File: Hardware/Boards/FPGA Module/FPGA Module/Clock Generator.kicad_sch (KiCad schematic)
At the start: 20 parts, among them U21 Si5338A-B-GMR, Y2 12Mhz

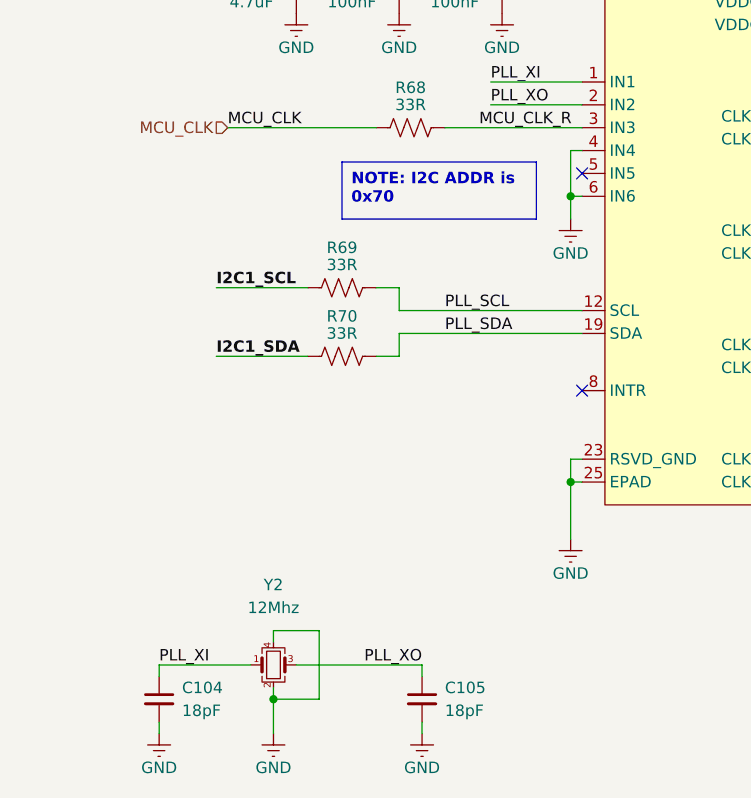
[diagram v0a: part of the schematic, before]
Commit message: updated fpga module schematics
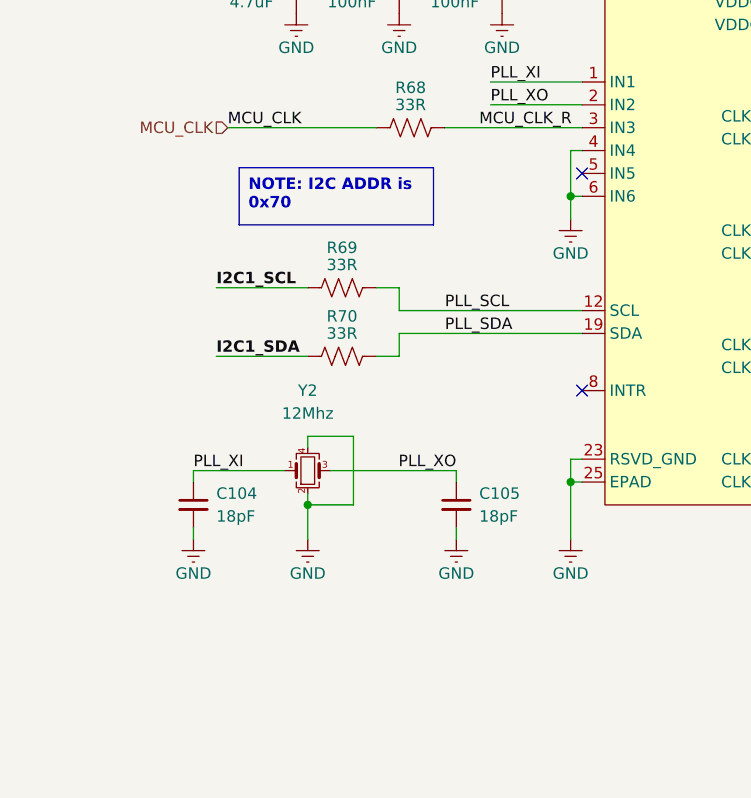
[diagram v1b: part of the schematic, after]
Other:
- moved on the sheet: C104, C105, Y2
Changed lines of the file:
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@@
 	)
 	(junction
-		(at 166.37 186.69)
+		(at 170.18 165.1)
 		(diameter 0)
 		(color 0 0 0 0)
@@
 	(wire
 		(pts
-			(xy 166.37 186.69) (xy 166.37 190.5)
+			(xy 170.18 165.1) (xy 170.18 168.91)
 		)
 		(stroke
@@
 	(wire
 		(pts
-			(xy 153.67 182.88) (xy 163.83 182.88)
+			(xy 157.48 161.29) (xy 167.64 161.29)
 		)
 		(stroke
@@
 	(wire
 		(pts
-			(xy 171.45 179.07) (xy 171.45 186.69)
+			(xy 175.26 157.48) (xy 175.26 165.1)
 		)
 		(stroke
@@
 	(wire
 		(pts
-			(xy 166.37 186.69) (xy 166.37 185.42)
+			(xy 170.18 165.1) (xy 170.18 163.83)
 		)
 		(stroke
@@
 	(wire
 		(pts
-			(xy 171.45 186.69) (xy 166.37 186.69)
+			(xy 175.26 165.1) (xy 170.18 165.1)
 		)
 		(stroke
@@
 	(wire
 		(pts
-			(xy 153.67 189.23) (xy 153.67 190.5)
+			(xy 157.48 167.64) (xy 157.48 168.91)
 		)
 		(stroke
@@
 	(wire
 		(pts
-			(xy 182.88 189.23) (xy 182.88 190.5)
+			(xy 186.69 167.64) (xy 186.69 168.91)
 		)
 		(stroke
@@
 	(wire
 		(pts
-			(xy 166.37 180.34) (xy 166.37 179.07)
+			(xy 170.18 158.75) (xy 170.18 157.48)
 		)
 		(stroke
@@
 	(wire
 		(pts
-			(xy 182.88 182.88) (xy 182.88 184.15)
+			(xy 186.69 161.29) (xy 186.69 162.56)
 		)
 		(stroke
@@
 	(wire
 		(pts
-			(xy 168.91 182.88) (xy 182.88 182.88)
+			(xy 172.72 161.29) (xy 186.69 161.29)
 		)
 		(stroke
@@
 	(wire
 		(pts
-			(xy 166.37 179.07) (xy 171.45 179.07)
+			(xy 170.18 157.48) (xy 175.26 157.48)
 		)
 		(stroke
@@
 	(wire
 		(pts
-			(xy 153.67 182.88) (xy 153.67 184.15)
+			(xy 157.48 161.29) (xy 157.48 162.56)
 		)
 		(stroke
@@
 	(text_box "NOTE: I2C ADDR is 0x70"
 		(exclude_from_sim no)
-		(at 173.99 127 0)
+		(at 162.56 127.635 0)
 		(size 21.59 6.35)
 		(stroke
@@
 	)
 	(label "PLL_XI"
-		(at 153.67 182.88 0)
+		(at 157.48 161.29 0)
 		(fields_autoplaced yes)
 		(effects
@@
 	)
 	(label "PLL_XO"
-		(at 182.88 182.88 180)
+		(at 186.69 161.29 180)
 		(fields_autoplaced yes)
 		(effects
@@
 	(symbol
 		(lib_id "Device:Crystal_GND24_Small")
-		(at 166.37 182.88 0)
+		(at 170.18 161.29 0)
 		(unit 1)
 		(exclude_from_sim no)
@@
 		(dnp no)
 		(property "Reference" "Y2"
-			(at 166.37 173.99 0)
+			(at 170.18 152.4 0)
 			(effects
 				(font
@@
 		)
 		(property "Value" "12Mhz"
-			(at 166.37 176.53 0)
+			(at 170.18 154.94 0)
 			(effects
 				(font
@@
 		)
 		(property "Footprint" "Oscillator:Oscillator_SMD_Abracon_ASE-4Pin_3.2x2.5mm"
-			(at 166.37 182.88 0)
+			(at 170.18 161.29 0)
 			(effects
 				(font
@@
 		)
 		(property "Datasheet" "https://abracon.com/Resonators/abm8.pdf"
-			(at 166.37 182.88 0)
+			(at 170.18 161.29 0)
 			(effects
 				(font
@@
 		)
 		(property "Description" "Four pin crystal, GND on pins 2 and 4, small symbol"
-			(at 166.37 182.88 0)
+			(at 170.18 161.29 0)
 			(effects
 				(font
@@
 	(symbol
 		(lib_id "Device:C_Small")
-		(at 182.88 186.69 0)
+		(at 186.69 165.1 0)
 		(unit 1)
 		(exclude_from_sim no)
@@
 		(fields_autoplaced yes)
 		(property "Reference" "C105"
-			(at 185.42 185.4262 0)
+			(at 189.23 163.8362 0)
 			(effects
 				(font
@@
 		)
 		(property "Value" "18pF"
-			(at 185.42 187.9662 0)
+			(at 189.23 166.3762 0)
 			(effects
 				(font
@@
 		)
 		(property "Footprint" "Capacitor_SMD:C_0201_0603Metric"
-			(at 182.88 186.69 0)
+			(at 186.69 165.1 0)
 			(effects
 				(font
@@
 		)
 		(property "Datasheet" "~"
-			(at 182.88 186.69 0)
+			(at 186.69 165.1 0)
 			(effects
 				(font
@@
 		)
 		(property "Description" "Unpolarized capacitor, small symbol"
-			(at 182.88 186.69 0)
+			(at 186.69 165.1 0)
 			(effects
 				(font
@@
 	(symbol
 		(lib_id "power:GND")
-		(at 153.67 190.5 0)
+		(at 157.48 168.91 0)
 		(unit 1)
 		(exclude_from_sim no)
@@
 		(dnp no)
 		(property "Reference" "#PWR0198"
-			(at 153.67 194.31 0)
+			(at 157.48 172.72 0)
 			(effects
 				(font
@@
 		)
 		(property "Value" "GND"
-			(at 153.67 194.31 0)
+			(at 157.48 172.72 0)
 			(effects
 				(font
@@
 		)
 		(property "Footprint" ""
-			(at 153.67 190.5 0)
+			(at 157.48 168.91 0)
 			(effects
 				(font
@@
 		)
 		(property "Datasheet" ""
-			(at 153.67 190.5 0)
+			(at 157.48 168.91 0)
 			(effects
 				(font
@@
 		)
 		(property "Description" "Power symbol creates a global label with name \"GND\" , ground"
-			(at 153.67 190.5 0)
+			(at 157.48 168.91 0)
 			(effects
 				(font
@@
 	(symbol
 		(lib_id "power:GND")
-		(at 182.88 190.5 0)
+		(at 186.69 168.91 0)
 		(unit 1)
 		(exclude_from_sim no)
@@
 		(dnp no)
 		(property "Reference" "#PWR0200"
-			(at 182.88 194.31 0)
+			(at 186.69 172.72 0)
 			(effects
 				(font
@@
 		)
 		(property "Value" "GND"
-			(at 182.88 194.31 0)
+			(at 186.69 172.72 0)
 			(effects
 				(font
@@
 		)
 		(property "Footprint" ""
-			(at 182.88 190.5 0)
+			(at 186.69 168.91 0)
 			(effects
 				(font
@@
 		)
 		(property "Datasheet" ""
-			(at 182.88 190.5 0)
+			(at 186.69 168.91 0)
 			(effects
 				(font
@@
 		)
 		(property "Description" "Power symbol creates a global label with name \"GND\" , ground"
-			(at 182.88 190.5 0)
+			(at 186.69 168.91 0)
 			(effects
 				(font
@@
 	(symbol
 		(lib_id "power:GND")
-		(at 166.37 190.5 0)
+		(at 170.18 168.91 0)
 		(unit 1)
 		(exclude_from_sim no)
@@
 		(dnp no)
 		(property "Reference" "#PWR0199"
-			(at 166.37 194.31 0)
+			(at 170.18 172.72 0)
 			(effects
 				(font
@@
 		)
 		(property "Value" "GND"
-			(at 166.37 194.31 0)
+			(at 170.18 172.72 0)
 			(effects
 				(font
@@
 		)
 		(property "Footprint" ""
-			(at 166.37 190.5 0)
+			(at 170.18 168.91 0)
 			(effects
 				(font
@@
 		)
 		(property "Datasheet" ""
-			(at 166.37 190.5 0)
+			(at 170.18 168.91 0)
 			(effects
 				(font
@@
 		)
 		(property "Description" "Power symbol creates a global label with name \"GND\" , ground"
-			(at 166.37 190.5 0)
+			(at 170.18 168.91 0)
 			(effects
 				(font
@@
 	(symbol
 		(lib_id "Device:C_Small")
-		(at 153.67 186.69 0)
+		(at 157.48 165.1 0)
 		(unit 1)
 		(exclude_from_sim no)
@@
 		(fields_autoplaced yes)
 		(property "Reference" "C104"
-			(at 156.21 185.4262 0)
+			(at 160.02 163.8362 0)
 			(effects
 				(font
@@
 		)
 		(property "Value" "18pF"
-			(at 156.21 187.9662 0)
+			(at 160.02 166.3762 0)
 			(effects
 				(font
@@
 		)
 		(property "Footprint" "Capacitor_SMD:C_0201_0603Metric"
-			(at 153.67 186.69 0)
+			(at 157.48 165.1 0)
 			(effects
 				(font
@@
 		)
 		(property "Datasheet" "~"
-			(at 153.67 186.69 0)
+			(at 157.48 165.1 0)
 			(effects
 				(font
@@
 		)
 		(property "Description" "Unpolarized capacitor, small symbol"
-			(at 153.67 186.69 0)
+			(at 157.48 165.1 0)
 			(effects
 				(font

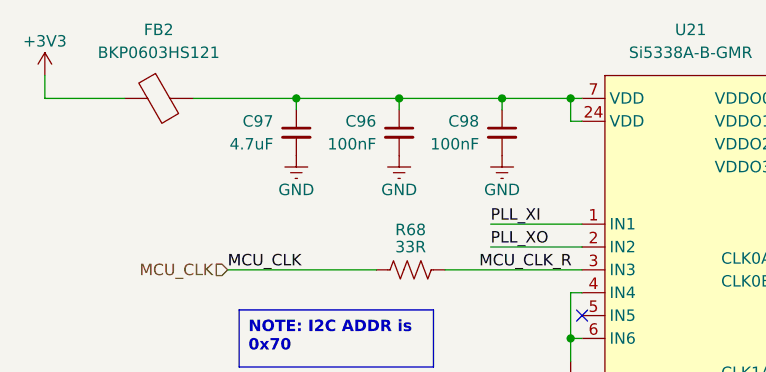
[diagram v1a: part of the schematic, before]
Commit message: Update FPGA Module Netclasses
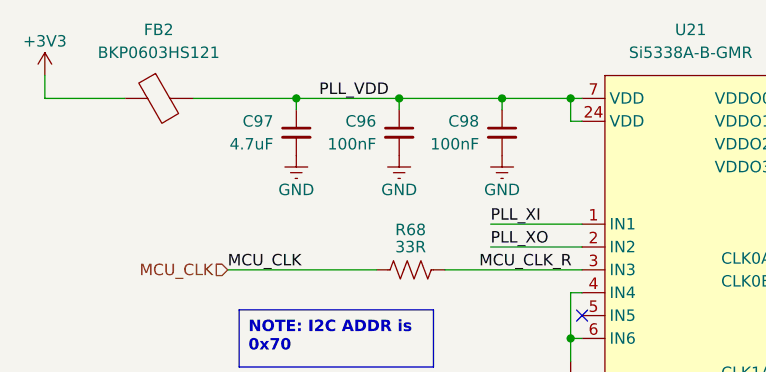
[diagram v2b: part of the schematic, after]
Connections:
- net PLL_VDD: now reaches C96.1, C97.1, C98.1, FB2.2, U21.24 (VDD), U21.7 (VDD)
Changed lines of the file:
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@@
+		)
+	)
+	(label "PLL_VDD"
+		(at 171.45 104.14 0)
+		(fields_autoplaced yes)
+		(effects
+			(font
+				(size 1.27 1.27)
+			)
+			(justify left bottom)
 		)
 	)

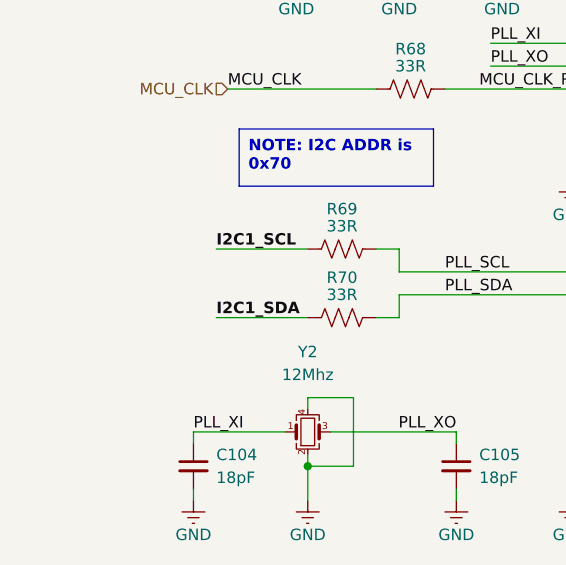
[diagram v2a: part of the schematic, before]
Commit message: Added Top sheet connections for FPGA module
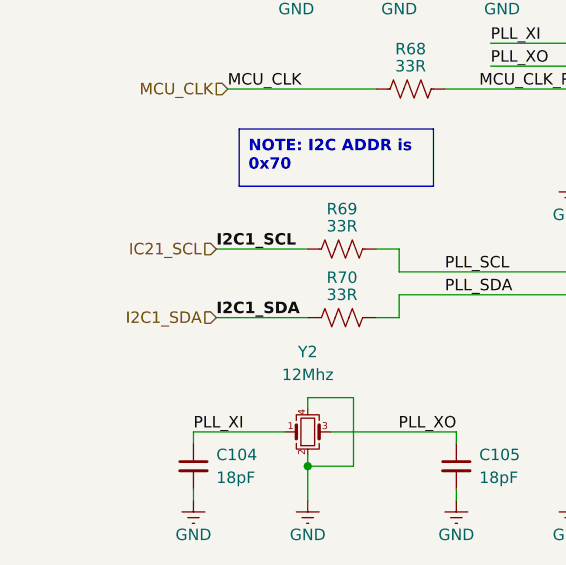
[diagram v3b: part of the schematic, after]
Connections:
- net I2C1_SCL renamed IC21_SCL
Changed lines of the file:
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@@
+		)
+	)
+	(hierarchical_label "I2C1_SDA"
+		(shape input)
+		(at 160.02 148.59 180)
+		(fields_autoplaced yes)
+		(effects
+			(font
+				(size 1.27 1.27)
+			)
+			(justify right)
 		)
 	)
@@
 		)
 	)
+	(hierarchical_label "IC21_SCL"
+		(shape input)
+		(at 160.02 140.97 180)
+		(fields_autoplaced yes)
+		(effects
+			(font
+				(size 1.27 1.27)
+			)
+			(justify right)
+		)
+	)

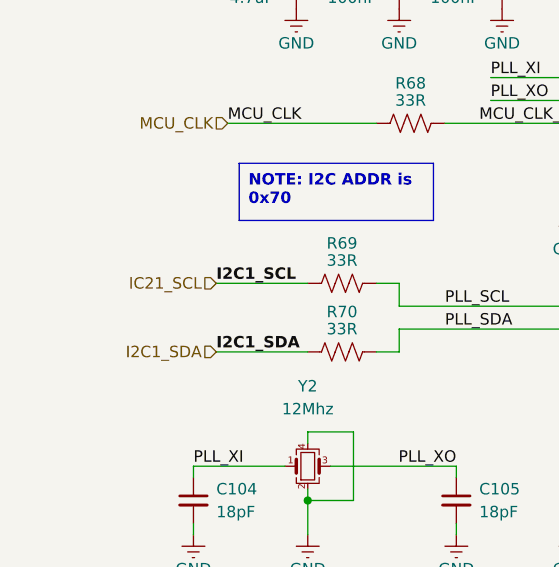
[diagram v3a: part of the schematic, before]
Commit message: Added NC to unused pins
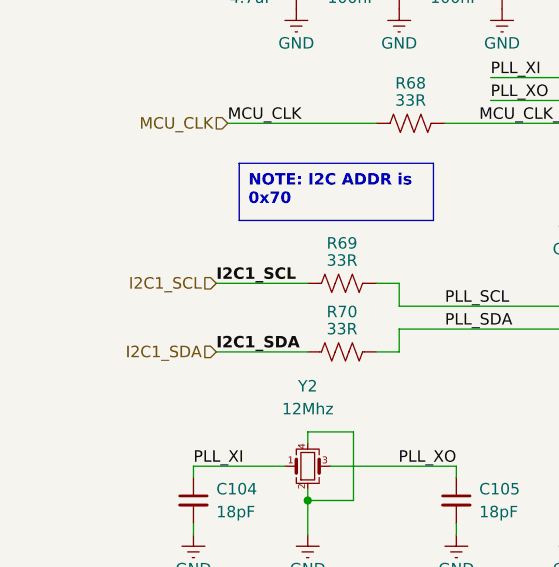
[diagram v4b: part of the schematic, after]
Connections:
- net IC21_SCL renamed I2C1_SCL
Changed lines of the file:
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@@
 		)
 	)
-	(hierarchical_label "IC21_SCL"
+	(hierarchical_label "I2C1_SCL"
 		(shape input)
 		(at 160.02 140.97 180)

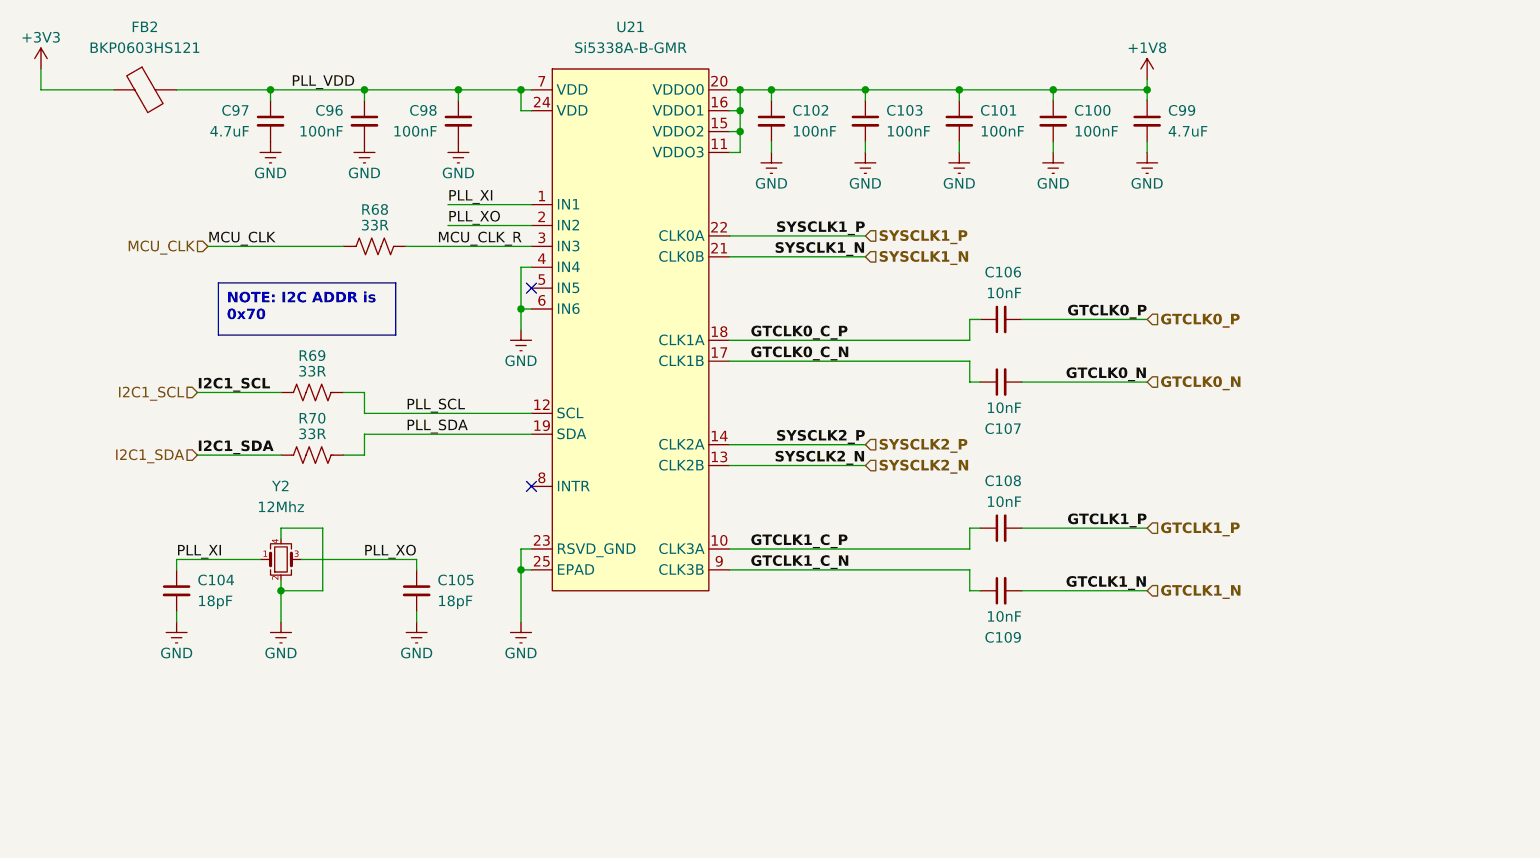
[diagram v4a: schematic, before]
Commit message: FPGA Module sch update
Added 3V3 LDO for MCU and 3V3 EN for DCDC. Also added SPI bus from MCU to FPGA with level shifter
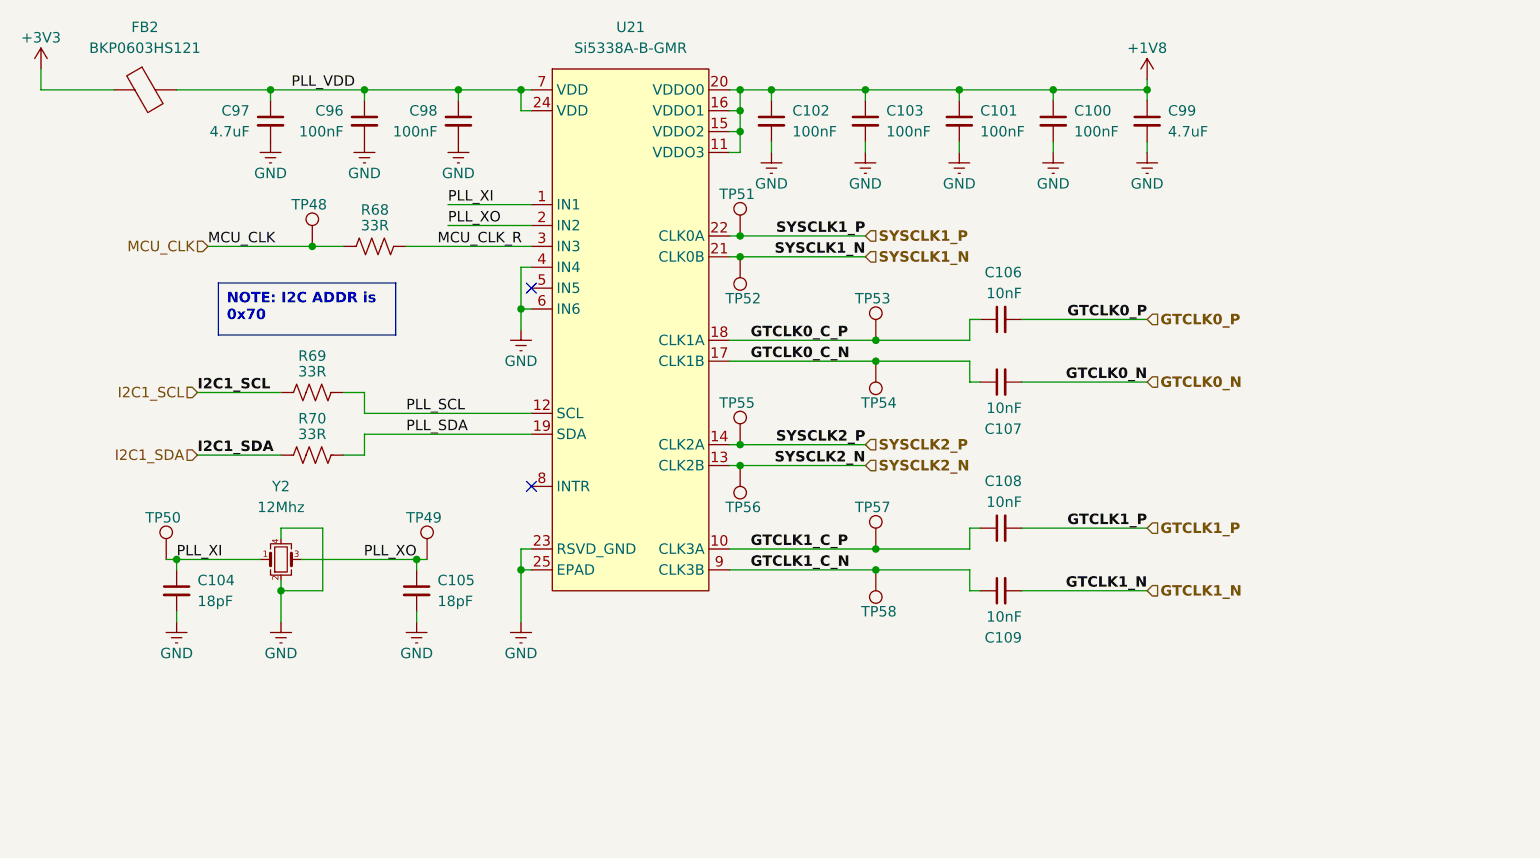
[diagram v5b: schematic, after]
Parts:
- added TP48, TP49, TP50, TP51, TP52, TP53, TP54, TP55, TP56, TP57, TP58: Test Point, FPGA Module:Test Point 0.75mm, symbol Connector:TestPoint
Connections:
- net GTCLK0_C_N: now also TP54.1
- net GTCLK0_C_P: now also TP53.1
- net GTCLK1_C_N: now also TP58.1
- net GTCLK1_C_P: now also TP57.1
- net MCU_CLK: now also TP48.1
- net PLL_XI: now also TP50.1
- net PLL_XO: now also TP49.1
- net SYSCLK1_N: now also TP52.1
- net SYSCLK1_P: now also TP51.1
- net SYSCLK2_N: now also TP56.1
- net SYSCLK2_P: now also TP55.1
